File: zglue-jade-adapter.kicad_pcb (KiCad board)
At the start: 8 copper layers, 25 x 20 mm, 63 parts, among them J1 543630489, J2 543630489, U1 zGlue-Jade

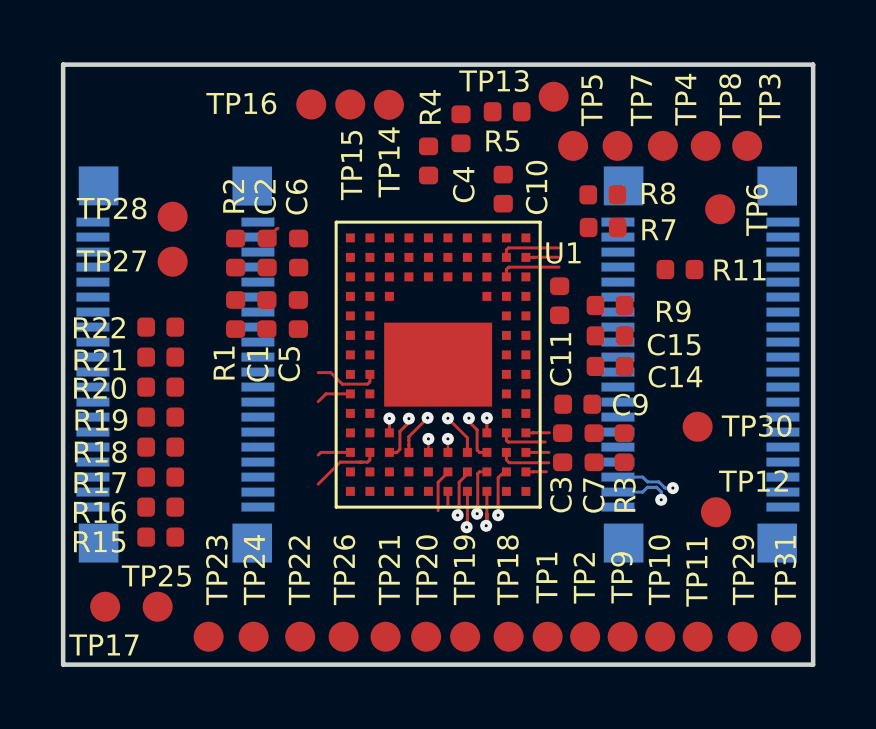
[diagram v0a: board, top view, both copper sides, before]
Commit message: Add LGA-96 step model, fix library links
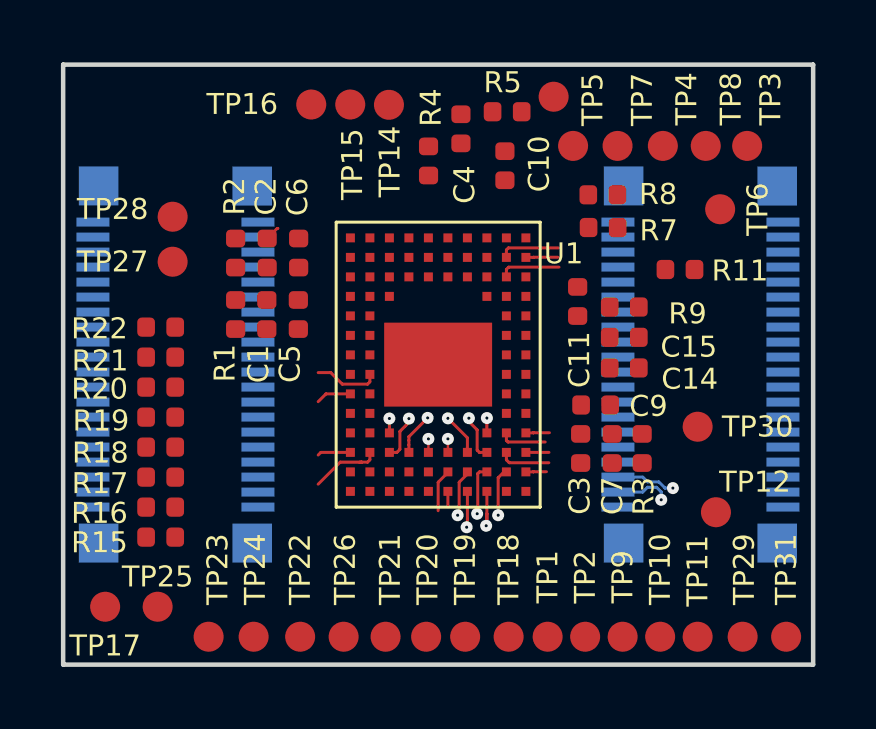
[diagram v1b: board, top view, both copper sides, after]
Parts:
- moved C10 0.78 mm to (14.7, 3.37)
- moved C3 0.60 mm to (17.2, 12.8)
- moved C7 0.60 mm to (18.3, 12.8)
- moved C9 0.60 mm to (17.8, 11.3)
- moved R3 0.60 mm to (19.3, 12.8)
- moved C11 0.60 mm to (17.1, 7.89)
- moved C15 0.48 mm to (18.7, 9.09)
- moved R9 0.48 mm to (18.7, 8.08)
- moved C14 0.48 mm to (18.7, 10.1)

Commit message: Rotate PCB by 180 deg to match chip logo orientation
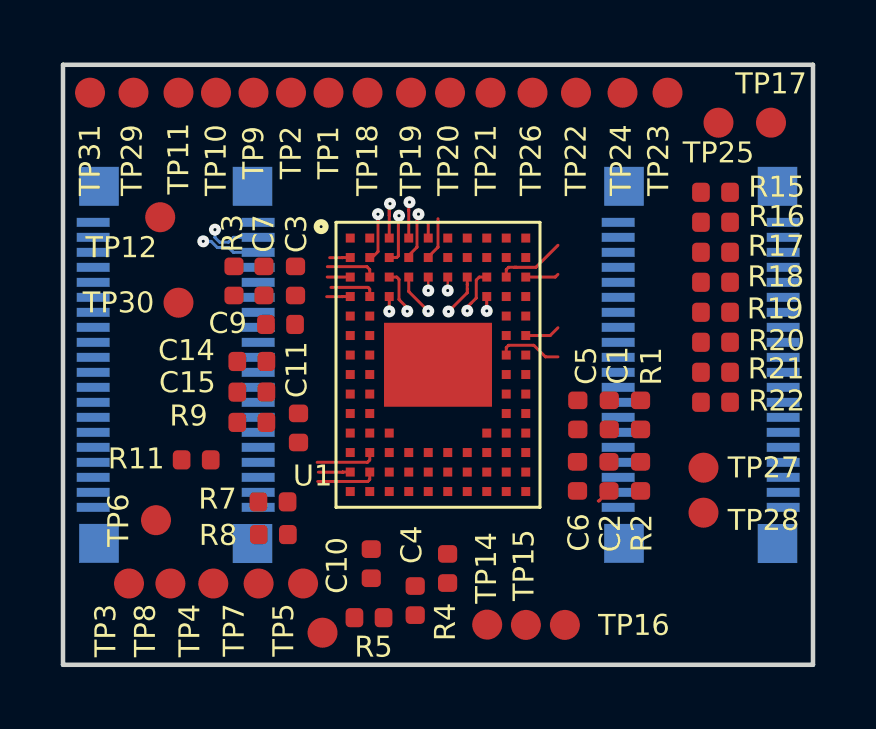
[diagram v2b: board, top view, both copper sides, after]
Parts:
- moved TP31 29.5 mm to (0.84, 0.94), turned to 270 degrees
- moved TP17 27.5 mm to (23.6, 1.88), turned to 180 degrees
- moved TP29 27.3 mm to (2.29, 0.94), turned to 270 degrees
- moved TP3 25.2 mm to (2.19, 17.2), turned to 180 degrees
- moved TP11 25.1 mm to (3.85, 0.88), turned to 180 degrees
- moved TP25 24.6 mm to (21.8, 1.94), turned to 270 degrees
- moved TP23 23.7 mm to (20.1, 0.94), turned to 270 degrees
- moved TP10 23.5 mm to (5.09, 0.88), turned to 180 degrees
- moved TP8 23.0 mm to (3.58, 17.2), turned to 180 degrees
- moved TP9 22.0 mm to (6.34, 0.88), turned to 180 degrees
- moved TP24 21.9 mm to (18.6, 0.94), turned to 270 degrees
- moved R15 21.8 mm to (21.7, 4.25), turned to 0 degrees
- moved TP6 21.6 mm to (3.04, 15.2), turned to 270 degrees
- moved TP12 21.0 mm to (3.23, 5.04), turned to 180 degrees
- moved TP4 20.8 mm to (5.00, 17.2), turned to 180 degrees
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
